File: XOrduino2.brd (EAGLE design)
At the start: 81.3 x 59.8 mm, 82 parts, among them J1 2.5mm, J2 2.5mm, J3 2.5mm, J4 2.5mm, J5 Batt In, J6 MOT R, J7 MOT L, P1 10k, Q1 ALS-PT204-6C/L177, SW1 RESET, SW2 6mm Button, SW3 LEFT BUMPER, SW4 RIGHT BUMPER, U1 ATMEGA32U4-XUAU, U2 LMV358, U3 NJU7261, U4 DRV8833PWP, U5 QRE1113GR, U6 QRE1113GR, X1 USBPCB, X2 USBMINIB, X3 USBMICROB-VIA, Y1 16MHz

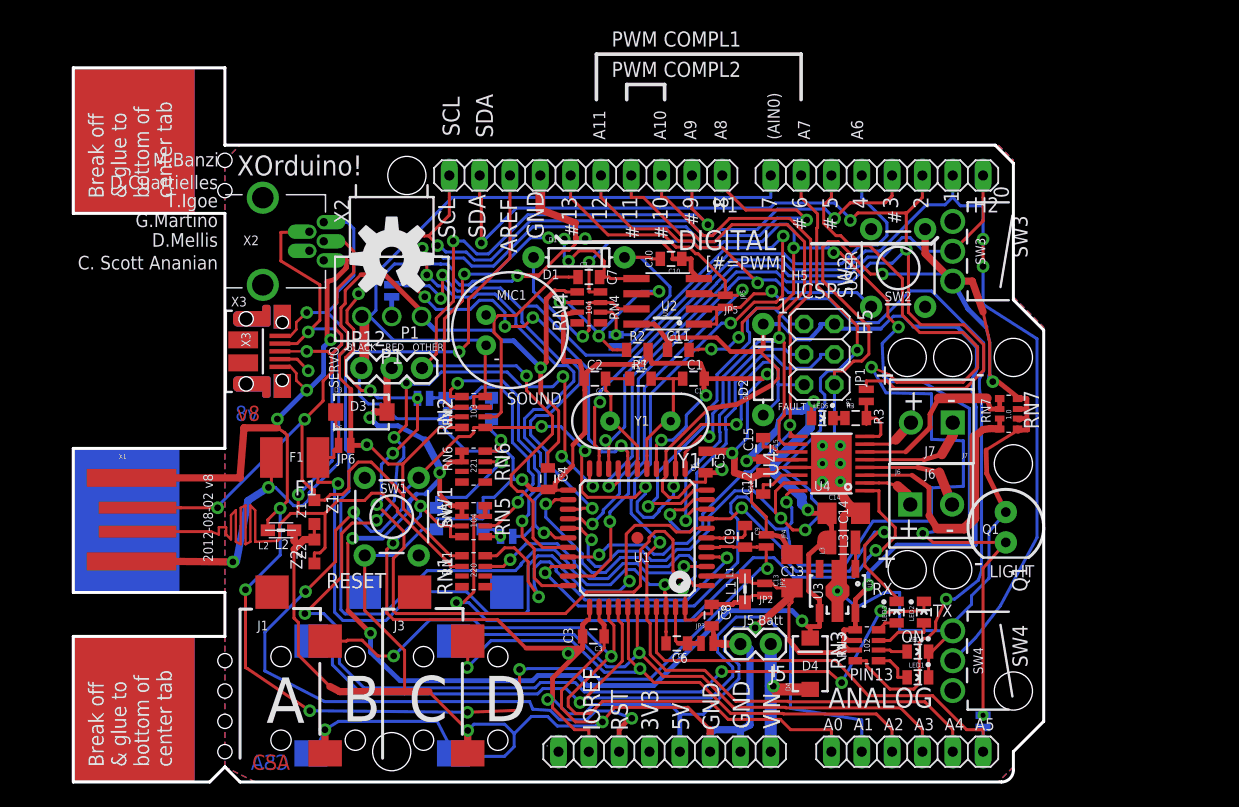
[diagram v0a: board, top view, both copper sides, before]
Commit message: all of second page deleted
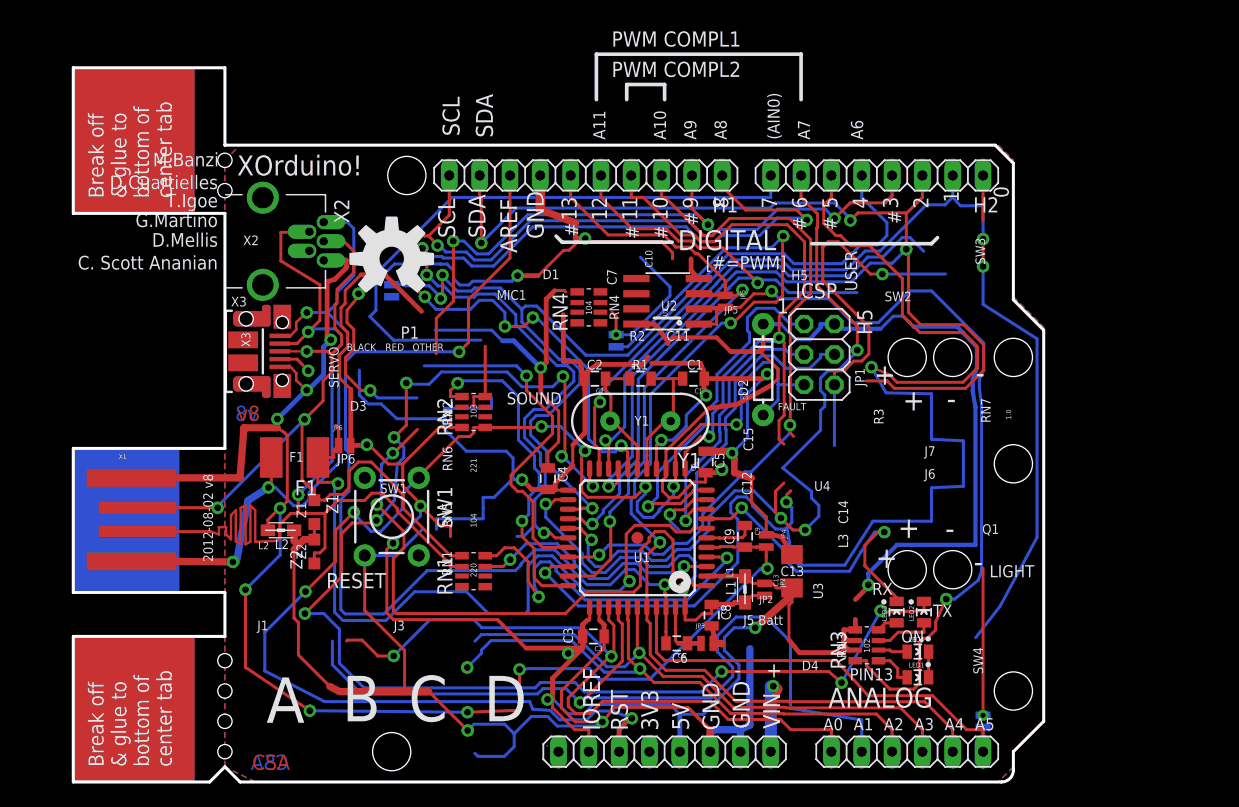
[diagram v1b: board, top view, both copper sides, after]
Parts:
- removed C10: 0.22uF, SparkFun-Passives:0805
- removed C11: 0.33uF, SparkFun-Passives:0805
- removed C12: 10uF, SparkFun-Passives:0805
- removed C14: 22uF, SparkFun-Passives:1206
- removed C15: 0.01uF, SparkFun-Passives:0805
- removed C7: 100n, SparkFun-Passives:0805
- removed D1: 1N4148, SparkFun-DiscreteSemi:DIODE-1N4148
- removed D3, D4: 1A Schottkey, SparkFun-DiscreteSemi:SMA-DIODE
- removed J1, J2, J3, J4: 2.5mm, xorduino:MJ-3523-SMT
- removed J5: Batt In, SparkFun-Connectors:1X02
- removed J6: MOT R, SparkFun:SCREWTERMINAL-3.5MM-2
- removed J7: MOT L, SparkFun:SCREWTERMINAL-3.5MM-2
- removed JP1: N/C, xorduino:SJ-2S-TRACE-NOCONFLICT
- removed JP10, JP11: N/C, xorduino:SJ-2S-BOT-TRACE-VIA-NOCONFLICT
- removed JP12: SERVO, SparkFun-Connectors:1X03
- removed L3: 100uH, SparkFun-Passives:1007
- removed LED5: FAULT Red, xorduino:LED0805
- removed MIC1: MIC9.7MM, SparkFun:MIC-9.7MM
- removed P1: 10k, xorduino:P091N
- removed Q1: ALS-PT204-6C/L177, xorduino:LED3MM-KIT
- removed R2: 2.2k, SparkFun-Passives:0805
- removed R3: 1k, SparkFun-Passives:0805
- removed RN5: 100k, xorduino:CRA06S
- removed RN6: 220, xorduino:CRA06S
- removed RN7: 1ohm 1/16W, resistor-dil:EXB38V
- removed SW2: 6mm Button, SparkFun-Electromechanical:TACTILE-PTH
- removed SW3: LEFT BUMPER, xorduino:SW-LEVER-V1-NOHOLES
- removed SW4: RIGHT BUMPER, xorduino:SW-LEVER-V2-NOHOLES
- removed U3: NJU7261, xorduino:SOT89-5
- removed U4: DRV8833PWP, xorduino:PWP16
- removed U5, U6: QRE1113GR, xorduino:QRE1113GR
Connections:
- removed net LED5_CATHODE: LED5.C, R3.1
- removed net MIC_IN: C7.1, MIC1.1, RN2.2
- removed net MOTL+: J7.2, U4.7
- removed net MOTL-: J7.1, U4.5
- removed net MOTR+: J6.1, U4.2
- removed net MOTR-: J6.2, U4.4
- removed net OPAMP1_M: R2.2, RN4.6, U2.6
- removed net OPAMP1_OUT: D1.A, RN4.3, U2.7
- removed net OPAMP1_P: C7.2, RN2.6, U2.5
- removed net U3_CONT: L3.2, U3.1
- removed net U4_AISEN: RN7.3, RN7.4, U4.3
- removed net U4_BISEN: RN7.1, RN7.2, U4.6
- removed net U4_NFAULT: JP1.1, R3.2, U4.8
- removed net U4_NSLEEP: RN5.7, RN5.8, U4.1
- removed net U4_VCP: C15.1, U4.11
- removed net U4_VINT: C12.1, U4.14
- removed net U5_ANODE: RN6.8, U5.1
- removed net U5_COLLECTOR: JP10.2, RN5.6, U5.3
- removed net U6_ANODE: RN6.7, U6.1
- removed net U6_COLLECTOR: JP11.1, JP11.VIA6, RN5.5, U6.3
- removed net VCCIO: C14.1, C15.2, D3.C, D4.C, JP12.2, L3.1, LED5.A, RN5.1, RN5.2, RN6.1, RN6.2, U3.4, U4.12
- net +5V: no longer C11.1, P1.1, RN2.7, RN4.5, RN5.3, RN5.4, U3.5
- net A0: no longer J1.2
- net A1: no longer J2.2
- net A2: no longer J3.2
- net A3: no longer J4.2
- net D0/RX: no longer SW3.NO
- net D1/TX: no longer SW4.NO
- net D2/SDA: no longer JP1.2
- net D5*: no longer U4.16
- net D6*: no longer U4.15
- net D7: no longer JP10.1, JP10.VIA6
- net GND: no longer C10.1, C12.2, C14.2, J1.1, J2.1, J3.1, J4.1, J5.2, JP12.1, MIC1.2, P1.3, Q1.A, R2.1, RN2.3, RN4.7, RN7.5, RN7.6, RN7.7, RN7.8, SW2.4, SW3.C, SW4.C, U3.2, U3.VIA1, U4.13, U4.PPAD, U4.VIA1, U4.VIA2, U4.VIA3, U4.VIA4, U4.VIA5, U4.VIA6, U5.2, U5.4, U6.2, U6.4
- net IO10*: no longer U4.9
- net IO11*: no longer U4.10
- net IO12: no longer SW2.1
- net IO8: no longer JP11.2
- net IO9*: no longer JP12.3
- net LIGHT: no longer C11.2, Q1.K, RN4.4
- net SLIDER: no longer P1.2
- net SOUND: no longer C10.2, D1.C, RN4.2
- net VIN: no longer D4.A, J5.1
- net VUSB: no longer D3.A
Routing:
- net GND: track 440.1 -> 307.4 mm, vias 12 -> 10
- net VCCIO: track 126.1 -> 0.00 mm, vias 8 -> 0
- net LIGHT: track 100.3 -> 12.3 mm, vias 7 -> 0
- net U4_NSLEEP: track 57.4 -> 0.00 mm, vias 2 -> 0
- net OPAMP1_P: track 32.9 -> 0.00 mm, vias 4 -> 0
- net U4_AISEN: track 22.9 -> 0.00 mm
- net U5_COLLECTOR: track 21.3 -> 0.00 mm, vias 1 -> 0
- net MIC_IN: track 18.8 -> 0.00 mm
- net OPAMP1_M: track 17.3 -> 0.00 mm, vias 3 -> 0
- net OPAMP1_OUT: track 15.8 -> 0.00 mm, vias 1 -> 0
- net U4_BISEN: track 15.6 -> 0.00 mm
- net MOTL-: track 9.42 -> 0.00 mm
- net MOTR-: track 9.18 -> 0.00 mm
- net U6_ANODE: track 8.94 -> 0.00 mm, vias 1 -> 0
- net +5V: track 268.6 -> 259.8 mm
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
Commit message: didn't select brd and sch together -- goes with last commit
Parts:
- removed H1: 10x1F-H8.5, SmartPrj:1X10
- removed H2, H3: 8x1F-H8.5, SmartPrj:1X08
- removed H4: 6x1F-H8.5, SmartPrj:1X06
- removed JP5: N/C, xorduino:SJ-2S-TRACE-NOCONFLICT
- removed JP7, JP8: N/C, xorduino:SJ-2S-BOT-TRACE-VIA-NOCONFLICT
- removed JP9: N/C, xorduino:SJ-2S-BOT-TRACE-NOCONFLICT
- removed LED1: L Yellow, xorduino:LED0805
- removed U$5: OSHW-LOGOL, SparkFun-Aesthetics:OSHW-LOGO-L
- removed X1: USBPCB, SparkFun-Connectors:USB-A-PCB
- removed X2: USBMINIB, xorduino:USB-MB-H2
- U2: value LMV358 -> LCD-16X2SILK; device SparkFun:SO08 -> SparkFun-Displays:LCD-16X2
- moved RN4 14.5 mm to (29.0, 36.7)
- moved U2 10.9 mm to (55.5, 31.0), turned to 0 degrees
- moved C2 7.31 mm to (41.5, 40.8)
- moved C1 6.99 mm to (51.7, 40.8)
- moved R1 6.75 mm to (47.0, 40.5)
- moved Y1 6.23 mm to (46.2, 36.3)
- moved C4 3.56 mm to (39.8, 29.0)
- moved C3 3.42 mm to (41.8, 15.1)
- moved U1 2.95 mm to (46.9, 23.4)
- moved C5 2.54 mm to (53.0, 29.3)
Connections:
- removed net +3V3: H3.4
- removed net IO13_MIRROR: JP5.2, RN3.8, U2.1, U2.2
- removed net LED1_ANODE: LED1.A, RN3.1
- removed net LIGHT: JP8.1, JP8.VIA6
- removed net SLIDER: JP9.1
- removed net SOUND: JP7.1, JP7.VIA6
- removed net VIN: H3.8
- new net A: U2.15
- new net K: U2.16
- new net VDD: U2.2
- new net VSS: U2.1
- net +5V: no longer H3.2, H3.5, U2.8
- net A0: no longer H4.1
- net A1: no longer H4.2
- net A2: no longer H4.3
- net A3: no longer H4.4
- net A4: no longer H4.5, JP7.2
- net A5: no longer H4.6, JP8.2
- net AREF: no longer H1.8
- net D0/RX: no longer H2.1
- net D1/TX: no longer H2.2
- net D2/SDA: no longer H1.9, H2.3
- net D3/SCL: no longer H1.10, H2.4
- net D4: no longer H2.5, JP9.2
- net D5*: no longer H2.6
- net D6*: no longer H2.7
- net D7: no longer H2.8
- net D_M: no longer X1.USB_M, X2.D-
- net D_P: no longer X1.USB_P, X2.D+
- net GND: no longer H1.7, H3.6, H3.7, LED1.C, U2.4
- net IO10*: no longer H1.3
- net IO11*: no longer H1.4
- net IO12: no longer H1.5
- net IO13*: no longer H1.6, JP5.1, U2.3
- net IO8: no longer H1.1
- net IO9*: no longer H1.2
- net RESET: no longer H3.3
- net UGND: no longer X1.GND, X2.GND
- net XUSB: no longer X1.5V, X2.VBUS
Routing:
- net GND: track 307.4 -> 0.00 mm, vias 10 -> 0
- net +5V: track 259.8 -> 0.00 mm, vias 9 -> 0
- net UGND: track 118.7 -> 0.00 mm, vias 8 -> 0
- net RESET: track 117.8 -> 0.00 mm, vias 8 -> 0
- net D2/SDA: track 116.2 -> 0.00 mm, vias 4 -> 0
- net TXLED: track 113.1 -> 0.00 mm, vias 10 -> 0
- net D5*: track 109.3 -> 0.00 mm, vias 3 -> 0
- net D7: track 106.7 -> 0.00 mm, vias 4 -> 0
- net A4: track 91.2 -> 0.00 mm, vias 3 -> 0
- net D1/TX: track 88.6 -> 0.00 mm, vias 3 -> 0
- net D_M: track 88.2 -> 0.00 mm, vias 1 -> 0
- net D3/SCL: track 88.0 -> 0.00 mm, vias 6 -> 0
- net IO8: track 84.9 -> 0.00 mm, vias 4 -> 0
- net AREF: track 84.5 -> 0.00 mm, vias 2 -> 0
- net D4: track 83.6 -> 0.00 mm, vias 3 -> 0
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- removed copper zone on layer 15, net +5V
- removed copper zone on layer 2, net GND
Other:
- board size 81.3 x 59.8 mm -> 68.6 x 53.3 mm
- board text removed: "#"
- board text removed: "& glue to"
- board text removed: "(AIN0)"
- board text removed: "-"
- board text removed: "0"
- board text removed: "10"
- board text removed: "11"
- board text removed: "12"
- board text removed: "13"
- board text removed: "2"
- board text removed: "2012-08-02 v8"
- board text removed: "221"
- board text removed: "3"
- board text removed: "3V3"
- board text removed: "4"
- board text removed: "4.5v"
- board text removed: "5"
- board text removed: "5V"
- board text removed: "6"
- board text removed: "7"
- board text removed: "8"
- board text removed: "9"
- board text removed: "A"
- board text removed: "A0"
- board text removed: "A1"
- board text removed: "A10"
- board text removed: "A11"
- board text removed: "A2"
- board text removed: "A3"
- board text removed: "A4"
- board text removed: "A6"
- board text removed: "A7"
- board text removed: "A8"
- board text removed: "A9"
- board text removed: "ANALOG"
- board text removed: "AREF"
- board text removed: "B"
- board text removed: "BLACK"
- board text removed: "Battery"
- board text removed: "Bottom"
- board text removed: "Break off"
- board text removed: "C"
- board text removed: "C. Scott Ananian"
- board text removed: "C10"
- board text removed: "C11"
- board text removed: "C14"
- board text removed: "CSA"
- board text removed: "Cut JP2 if populating L1"
- board text removed: "Cut JP5 if populating U2"
- board text removed: "Cut JP6 if populating U3"
- board text removed: "D"
- board text removed: "D.Cuartielles"
- board text removed: "D.Mellis"
- board text removed: "D1"
- board text removed: "D3"
- board text removed: "D4"
- board text removed: "DIGITAL"
- board text removed: "G.Martino"
- board text removed: "GND"
- board text removed: "H5"
- board text removed: "IOREF"
- board text removed: "J1"
- board text removed: "J2"
- board text removed: "J3"
- board text removed: "J4"
- board text removed: "J6"
- board text removed: "J7"
- board text removed: "JP10"
- board text removed: "JP11"
- board text removed: "M.Banzi"
- board text removed: "MIC1"
- board text removed: "Motors"
- board text removed: "OLPC-F"
- board text removed: "OTHER"
- board text removed: "P1"
- board text removed: "PIN13"
- board text removed: "PWM COMPL1"
- board text removed: "PWM COMPL2"
- board text removed: "R3"
- board text removed: "RED"
- board text removed: "RN5"
- board text removed: "RN6"
- board text removed: "RST"
- board text removed: "RX1"
- board text removed: "SCL"
- board text removed: "SDA"
- board text removed: "SERVO"
- board text removed: "SOUND"
- board text removed: "SW2"
- board text removed: "SW3"
- board text removed: "SW4"
- board text removed: "Sensors"
- board text removed: "Speed"
- board text removed: "T.Igoe"
- board text removed: "TX1"
- board text removed: "U2"
- board text removed: "U4"
- board text removed: "U6"
- board text removed: "USER"
- board text removed: "VIN"
- board text removed: "X"
- board text removed: "X2"
- board text removed: "XOrduino!"
- board text removed: "[#=PWM]"
- board text removed: "bottom of"
- board text removed: "center tab"
- board text removed: "o"

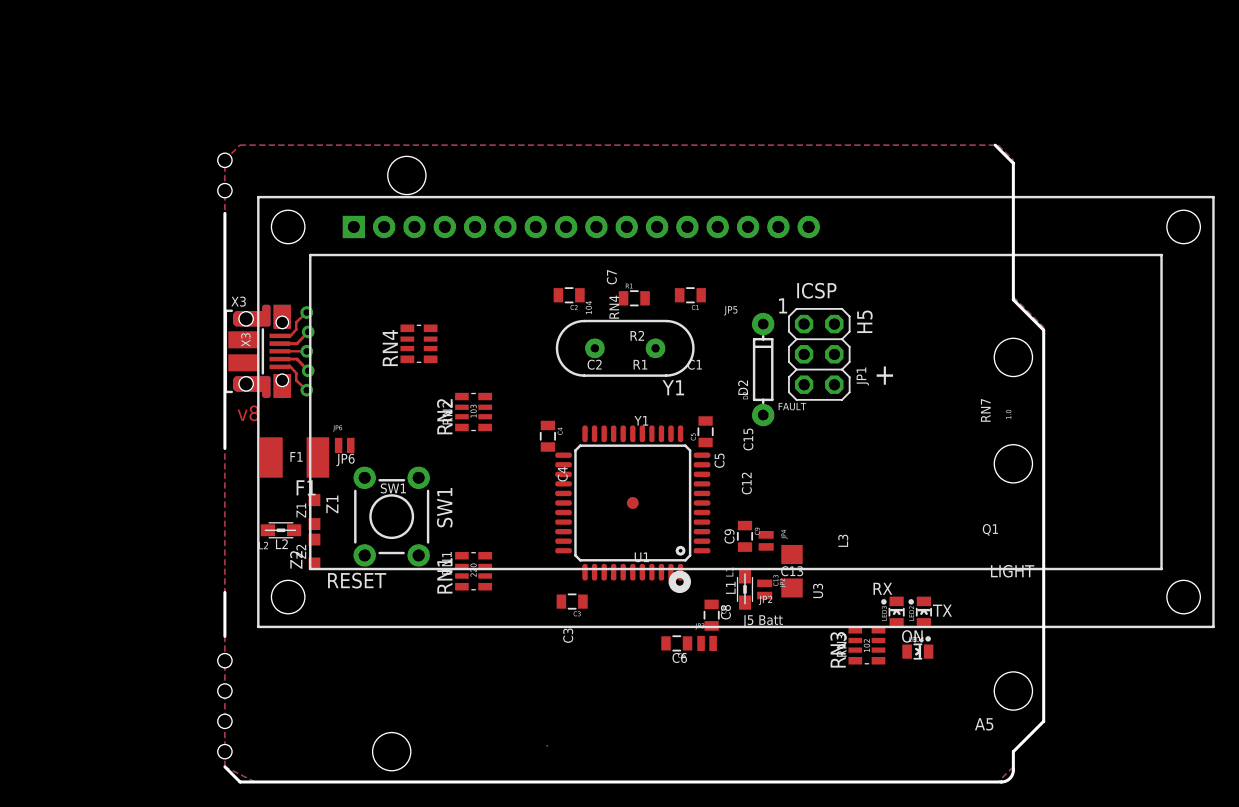
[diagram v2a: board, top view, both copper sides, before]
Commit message: starting to eliminate vias, work with component orientation
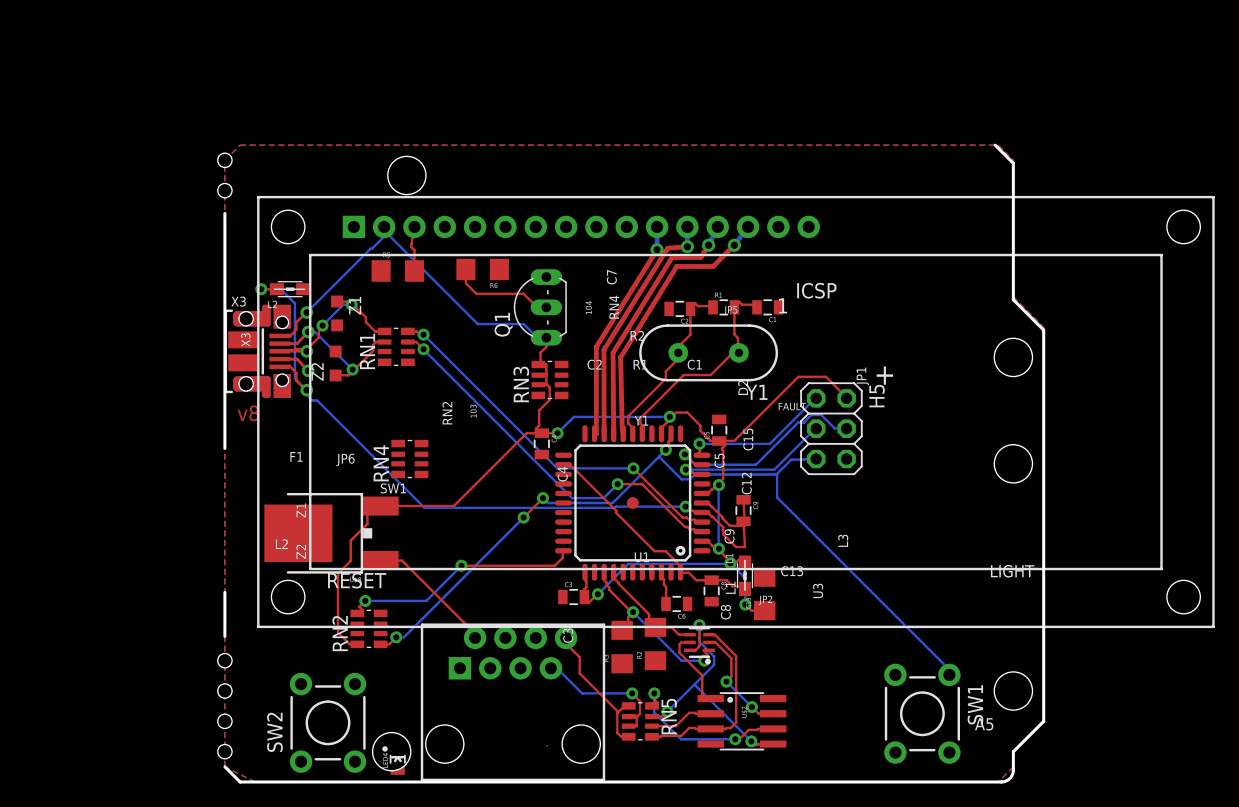
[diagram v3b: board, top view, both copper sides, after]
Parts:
- removed D2: 1N4148, SparkFun-DiscreteSemi:DIODE-1N4148
- removed F1: 0ZCC0110FF2C 1.1A, rcl:L1812
- removed JP2, JP3, JP4, JP6: N/C, xorduino:SJ-2S-TRACE-NOCONFLICT
- removed LED2: TX Red, xorduino:LED0805
- removed LED3: RX Red, xorduino:LED0805
- added Q1: 2N2907, adafruit:TO92-EBC-OVAL
- added R2, R3, R5, R6: (no value), SparkFun-Passives:1206
- added RN5: 22, xorduino:CRA06S
- added SW2: RESET, SparkFun-Electromechanical:TACTILE-PTH
- added U$2: LMV358, SparkFun-AnalogIC:SO08
- added U$5: MMDT3904, SparkFun-DiscreteSemi:SOT363
- added U$6: RJ45-8PTH, SparkFun-Connectors:RJ45-8
- added U$8: LM2931_FIXED, SparkFun-PowerIC:DPAK
- moved SW1 47.4 mm to (71.1, 5.71)
- moved LED4 44.5 mm to (27.2, 1.91), turned to 90 degrees
- moved RN3 34.6 mm to (39.9, 33.7)
- moved L2 20.2 mm to (18.2, 41.3)
- moved RN2 20.2 mm to (24.8, 12.8)
- moved RN1 19.9 mm to (27.1, 36.4)
- moved Z1 16.7 mm to (22.1, 39.2)
- moved Z2 15.8 mm to (22.0, 35.1)
- moved RN4 9.68 mm to (28.2, 27.1)
- moved C2 9.34 mm to (50.8, 39.6)
- moved R1 7.53 mm to (54.5, 39.8)
- moved Y1 7.00 mm to (53.2, 35.9)
- moved C1 6.56 mm to (58.2, 39.8)
- moved H5 6.31 mm to (63.5, 29.6)
- moved C6 3.30 mm to (50.5, 14.9)
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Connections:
- net A renamed N$13
- removed net K: U2.16
- removed net VDD: U2.2
- removed net VSS: U2.1
- removed net VUSB: F1.1, JP6.1, U1.7
- removed net XUSB: F1.2, X3.VBUS, X3.VBUS_VIA
- new net +V: U$2.8
- new net N$1: RN5.5, U$2.3, U$5.3
- new net N$12: R5.2, U2.3
- new net N$14: Q1.B, R6.2
- new net N$18: U$6.2, U$8.1
- new net N$2: RN5.8, U$2.6
- new net N$3: RN5.7, U$2.5, U$5.6
- new net N$4: U$2.1, U$5.5
- new net N$5: U$2.7, U$5.2
- new net N$6: RN5.6, U$2.2
- new net N$7: RN5.1, RN5.4, U$6.8
- new net N$8: RN5.2, RN5.3, U$6.7
- net +5V: now also Q1.E, U$8.3, U1.7, U2.2, X3.VBUS, X3.VBUS_VIA; no longer D2.C, JP2.1, JP6.2
- net A0: now also R3.2, U$5.1
- net A1: now also R2.2, U$5.4
- net AGND: no longer C6.1, JP3.1
- net AVCC: no longer JP2.2
- net D0/RX: now also U2.12
- net D1/TX: now also U2.11
- net D2/SDA: now also U2.13
- net D3/SCL: now also U2.14
- net GND: now also C6.1, R2.1, R3.1, R5.1, U$2.4, U$6.1, U$8.4, U2.1, U2.16, U2.5; no longer JP3.2, JP4.1
- net LED2_ANODE: no longer LED2.A
- net LED3_ANODE: no longer LED3.A
- net RESET: no longer D2.A
- net RXLED: no longer LED3.C
- net TXLED: no longer LED2.C
- net UGND: no longer JP4.2
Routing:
- net +5V: track 0.00 -> 140.7 mm, vias 0 -> 7
- net RESET: track 0.00 -> 70.0 mm, vias 0 -> 4
- net UGND: track 0.00 -> 57.4 mm, vias 0 -> 2
- net RD_M: track 0.00 -> 32.2 mm, vias 0 -> 2
- net RD_P: track 0.00 -> 31.3 mm, vias 0 -> 2
- net D3/SCL: track 0.00 -> 22.8 mm, vias 0 -> 1
- net N$3: track 0.00 -> 22.4 mm, vias 0 -> 3
- net D2/SDA: track 0.00 -> 21.5 mm, vias 0 -> 1
- net HWB: track 0.00 -> 20.5 mm, vias 0 -> 2
- net D0/RX: track 0.00 -> 20.4 mm, vias 0 -> 1
- net AVCC: track 0.00 -> 20.0 mm
- net D1/TX: track 0.00 -> 18.9 mm, vias 0 -> 1
- net XTAL2: track 0.00 -> 18.6 mm
- net MOSI: track 0.00 -> 17.9 mm, vias 0 -> 1
- net N$1: track 0.00 -> 16.2 mm
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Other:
- board text removed: "1.0"
- board text removed: "102"
- board text removed: "220"
- board text removed: "Alt Routing for LIGHT/A5"
- board text removed: "C6"
- board text removed: "Front Skid"
- board text removed: "J5 Batt"
- board text removed: "ON"
- board text removed: "Q1"
- board text removed: "RN1"
- board text removed: "RN3"
- board text removed: "RN7"
- board text removed: "RX"
- board text removed: "TX"
